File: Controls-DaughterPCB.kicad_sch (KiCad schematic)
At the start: 23 parts, among them U8 LMC555xM

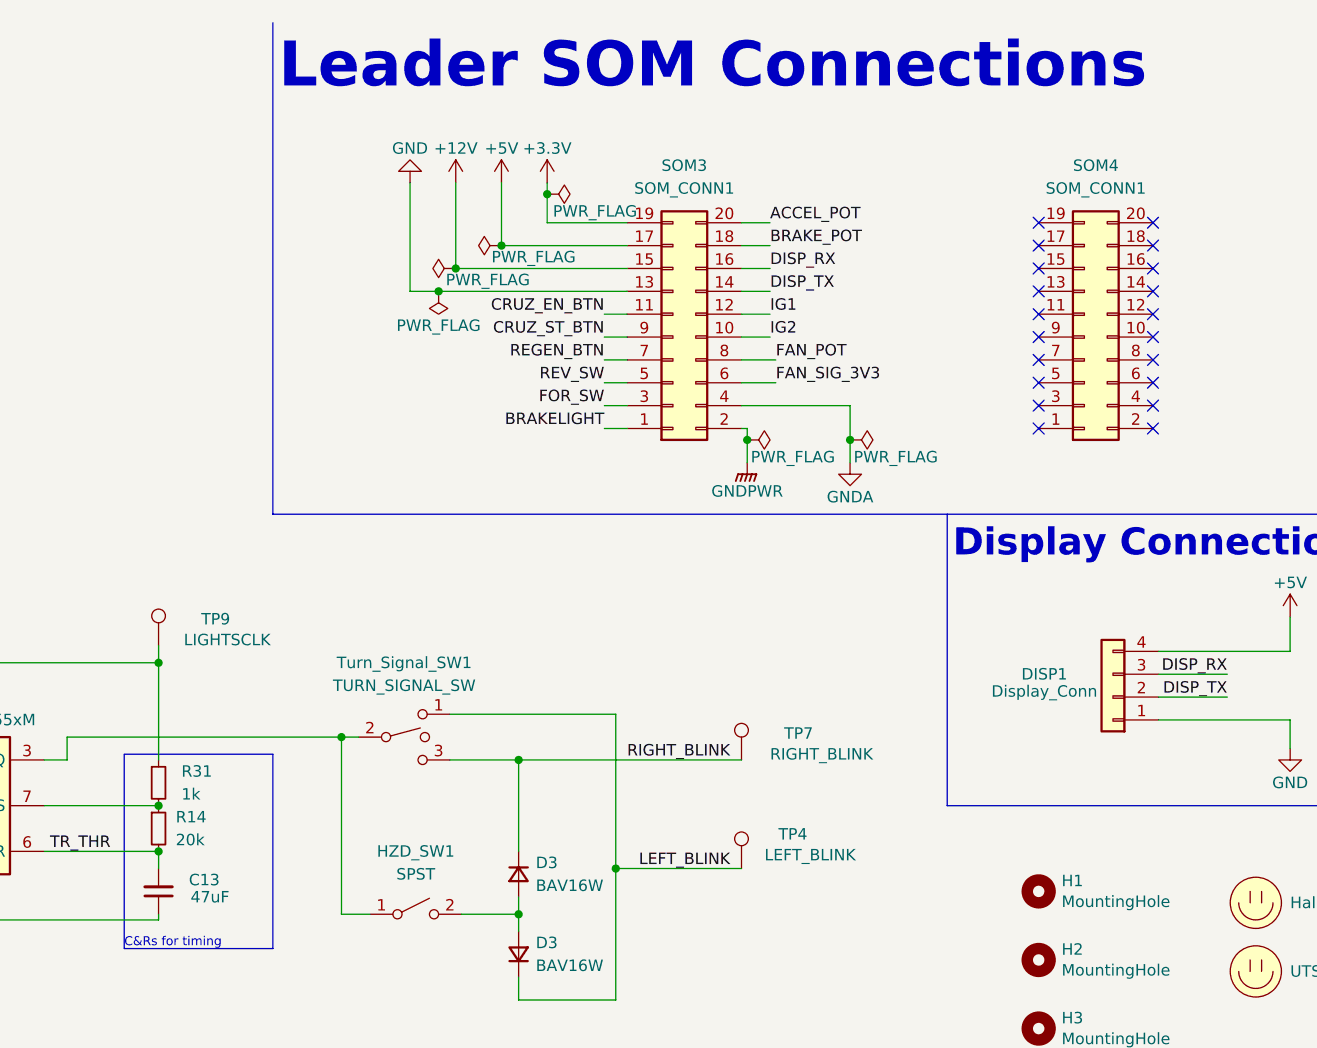
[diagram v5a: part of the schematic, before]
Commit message: changed labels for some connectors
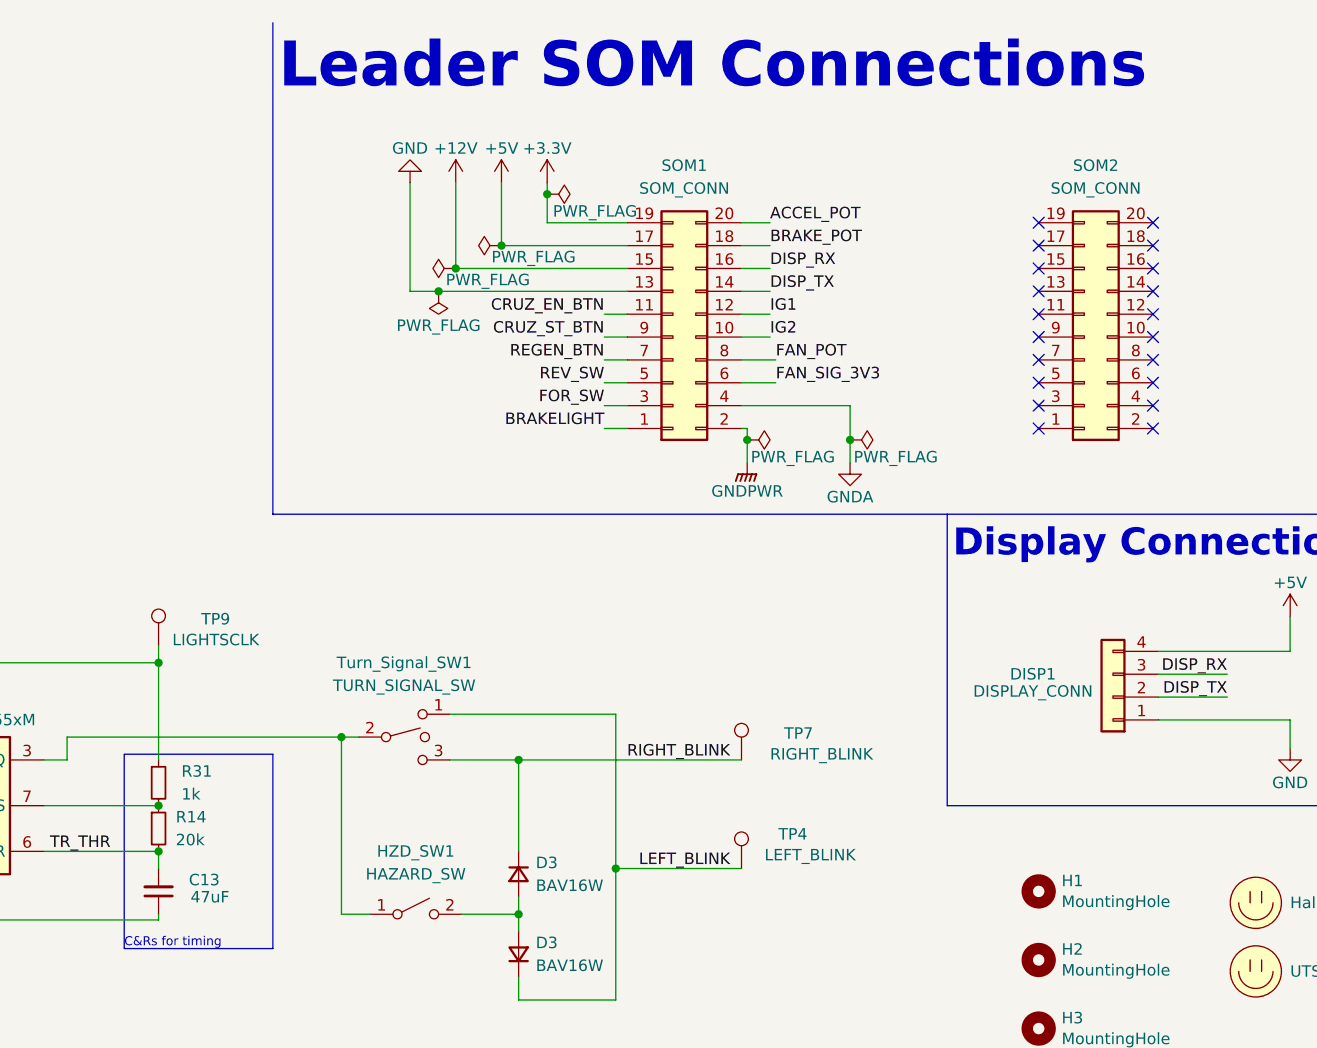
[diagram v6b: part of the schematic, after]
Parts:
- DISP1: value Display_Conn -> DISPLAY_CONN
- HZD_SW1: value SPST -> HAZARD_SW
- SOM1: renamed from SOM3; value SOM_CONN1 -> SOM_CONN
- SOM2: renamed from SOM4; value SOM_CONN1 -> SOM_CONN
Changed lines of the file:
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@@
       (effects (font (size 1.27 1.27)))
     )
-    (property "Value" "SPST" (at 176.53 106.045 0)
+    (property "Value" "HAZARD_SW" (at 176.53 106.045 0)
       (effects (font (size 1.27 1.27)))
     )
@@
       (project "Controls-DaughterPCB"
         (path "/c7871779-04fe-4705-8150-20a4dd0ef44f"
-          (reference "HZD_SW2") (unit 1)
+          (reference "HZD1") (unit 1)
         )
       )
@@
       (project "Controls-DaughterPCB"
         (path "/c7871779-04fe-4705-8150-20a4dd0ef44f"
-          (reference "Turn_Signal_SW2") (unit 1)
+          (reference "TURN_SIG1") (unit 1)
         )
       )
@@
   (symbol (lib_id "Connector_Generic:Conn_02x10_Odd_Even") (at 205.105 46.355 0) (mirror x) (unit 1)
     (in_bom yes) (on_board yes) (dnp no)
-    (property "Reference" "SOM3" (at 206.375 27.305 0)
-      (effects (font (size 1.27 1.27)))
-    )
-    (property "Value" "SOM_CONN1" (at 206.375 29.845 0)
+    (property "Reference" "SOM1" (at 206.375 27.305 0)
+      (effects (font (size 1.27 1.27)))
+    )
+    (property "Value" "SOM_CONN" (at 206.375 29.845 0)
       (effects (font (size 1.27 1.27)))
     )
@@
       (project "Controls-DaughterPCB"
         (path "/c7871779-04fe-4705-8150-20a4dd0ef44f"
-          (reference "SOM3") (unit 1)
+          (reference "SOM1") (unit 1)
         )
       )
@@
   (symbol (lib_id "Connector_Generic:Conn_01x04") (at 254 86.36 180) (unit 1)
     (in_bom yes) (on_board yes) (dnp no)
-    (property "Reference" "DISP1" (at 246.38 83.82 0)
-      (effects (font (size 1.27 1.27)))
-    )
-    (property "Value" "Display_Conn" (at 246.38 85.725 0)
+    (property "Reference" "DISP1" (at 245.11 83.82 0)
+      (effects (font (size 1.27 1.27)))
+    )
+    (property "Value" "DISPLAY_CONN" (at 245.11 85.725 0)
       (effects (font (size 1.27 1.27)))
     )
@@
   (symbol (lib_id "Connector_Generic:Conn_02x10_Odd_Even") (at 250.825 46.355 0) (mirror x) (unit 1)
     (in_bom yes) (on_board yes) (dnp no)
-    (property "Reference" "SOM4" (at 252.095 27.305 0)
-      (effects (font (size 1.27 1.27)))
-    )
-    (property "Value" "SOM_CONN1" (at 252.095 29.845 0)
+    (property "Reference" "SOM2" (at 252.095 27.305 0)
+      (effects (font (size 1.27 1.27)))
+    )
+    (property "Value" "SOM_CONN" (at 252.095 29.845 0)
       (effects (font (size 1.27 1.27)))
     )
@@
       (project "Controls-DaughterPCB"
         (path "/c7871779-04fe-4705-8150-20a4dd0ef44f"
-          (reference "SOM4") (unit 1)
+          (reference "SOM2") (unit 1)
         )
       )
@@
       (effects (font (size 1.27 1.27)))
     )
-    (property "Value" "LIGHTSCLK" (at 155.575 80.01 0)
-      (effects (font (size 1.27 1.27)))
-    )
+    (property "Value" "LIGHTSCLK" (at 154.305 80.01 0)
+      (effects (font (size 1.27 1.27)))
+    )
